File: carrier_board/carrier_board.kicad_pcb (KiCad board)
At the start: 2 copper layers, 40 x 68.9 mm, 10 parts, among them J1 47571-0001, U1 Pico

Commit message: Change red LED from GP2 to GP4 to free up UART RX
Also add label to LED on board
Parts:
- turned R1 to 90 degrees
- turned D1 to -90 degrees
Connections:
- D1 pad 1: Net-(D1-Pad1) -> GND
- D1 pad 2: Net-(D1-Pad2) -> Net-(R1-Pad2)
- R1 pad 1: Net-(D1-Pad1) -> Net-(U1-Pad6)
- R1 pad 2: GND -> Net-(R1-Pad2)
- U1 pad 2: Net-(D1-Pad2) -> unconnected-(U1-Pad2)
- U1 pad 6: unconnected-(U1-Pad6) -> Net-(U1-Pad6)
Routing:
- net Net-(D1-Pad2): track 9.67 -> 0.00 mm
- net Net-(U1-Pad6): track 0.00 -> 8.39 mm
- net Net-(R1-Pad2): track 0.00 -> 3.25 mm
- net Net-(D1-Pad1): track 3.21 -> 0.00 mm
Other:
- board text added: "OpenReset Carrier Board v1a caralynx 2022"
- board text removed: "OpenReset Carrier Board v1 caralynx 2022"

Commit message: Fix weird 3v3 routing
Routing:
- net VDD: track 55.9 -> 54.5 mm, vias 2 -> 1
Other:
- board text added: "OpenReset Carrier Board v1b caralynx 2022"
- board text removed: "OpenReset Carrier Board v1a caralynx 2022"
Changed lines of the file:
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@@
     (title "OpenReset Carrier Board")
     (date "2022-03-20")
-    (rev "v1a")
+    (rev "v1b")
     (company "cyanic")
   )
@@
   )
   (gr_rect (start 127 59) (end 167 127.9) (layer "Edge.Cuts") (width 0.1) (fill none))
-  (gr_text "OpenReset Carrier Board v1a\ncaralynx 2022" (at 147 120) (layer "B.SilkS")
+  (gr_text "OpenReset Carrier Board v1b\ncaralynx 2022" (at 147 120) (layer "B.SilkS")
     (effects (font (size 1 1) (thickness 0.15)) (justify mirror))
   )
@@
   (segment (start 151.8 117) (end 163 117) (width 0.25) (layer "F.Cu") (net 5))
   (segment (start 164 116) (end 164 101) (width 0.25) (layer "F.Cu") (net 5))
-  (segment (start 153.695 71.305) (end 153 72) (width 0.25) (layer "F.Cu") (net 6))
   (segment (start 153 116) (end 151 116) (width 0.25) (layer "F.Cu") (net 6))
   (segment (start 147.39 119.61) (end 147.39 121.06) (width 0.25) (layer "F.Cu") (net 6))
-  (segment (start 156.08 71.305) (end 153.695 71.305) (width 0.25) (layer "F.Cu") (net 6))
   (segment (start 151 116) (end 147.39 119.61) (width 0.25) (layer "F.Cu") (net 6))
   (via (at 153 116) (size 0.8) (drill 0.4) (layers "F.Cu" "B.Cu") (net 6))
-  (via (at 153 72) (size 0.8) (drill 0.4) (layers "F.Cu" "B.Cu") (net 6))
-  (segment (start 153 116) (end 153 72) (width 0.25) (layer "B.Cu") (net 6))
+  (segment (start 153 74.385) (end 153 116) (width 0.25) (layer "B.Cu") (net 6))
+  (segment (start 156.08 71.305) (end 153 74.385) (width 0.25) (layer "B.Cu") (net 6))
   (segment (start 161.785 101.785) (end 156.08 101.785) (width 0.25) (layer "F.Cu") (net 7))
   (segment (start 151 115) (end 162 115) (width 0.25) (layer "F.Cu") (net 7))

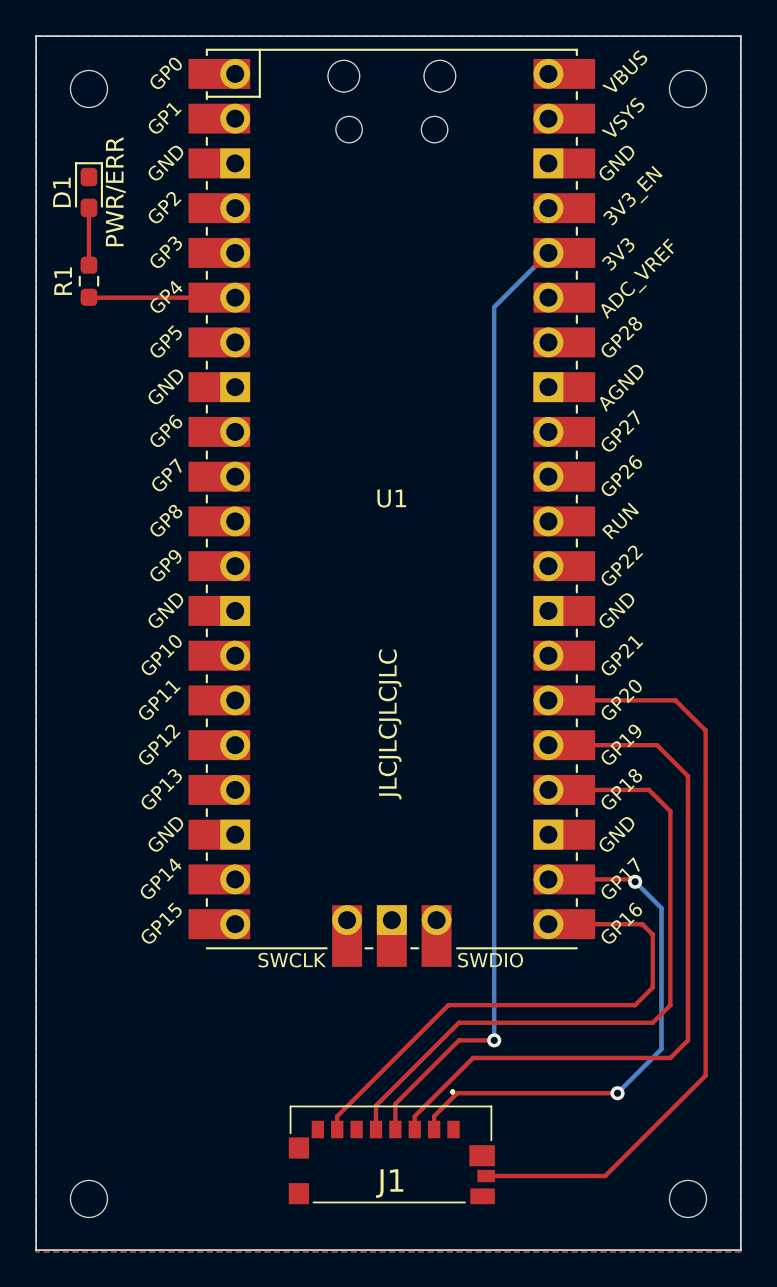
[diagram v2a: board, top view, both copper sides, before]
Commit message: Thicken power trace
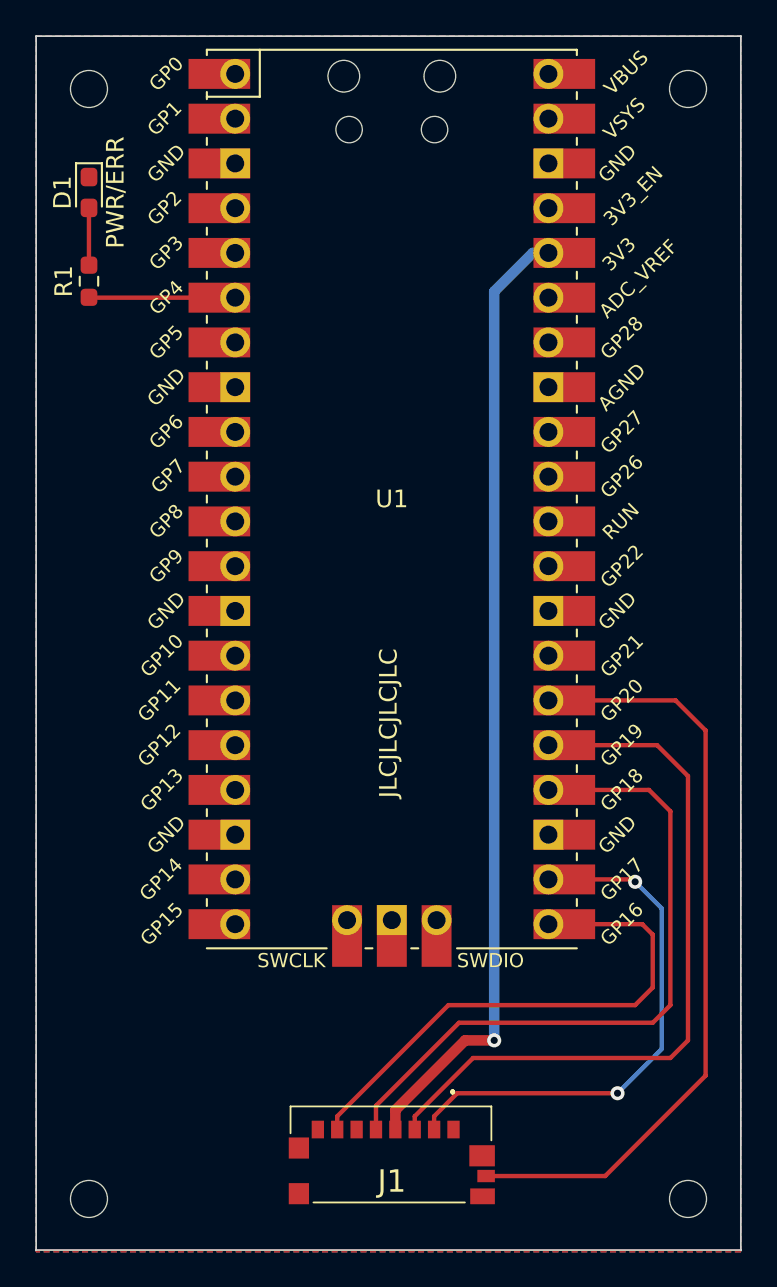
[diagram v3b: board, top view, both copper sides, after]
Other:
- board text added: "OpenReset Carrier Board v1c caralynx 2022"
- board text removed: "OpenReset Carrier Board v1b caralynx 2022"
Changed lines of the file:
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@@
   )
   (gr_rect (start 127 59) (end 167 127.9) (layer "Edge.Cuts") (width 0.1) (fill none))
-  (gr_text "OpenReset Carrier Board v1b\ncaralynx 2022" (at 147 120) (layer "B.SilkS")
+  (gr_text "OpenReset Carrier Board v1c\ncaralynx 2022" (at 147 120) (layer "B.SilkS")
     (effects (font (size 1 1) (thickness 0.15)) (justify mirror))
   )
@@
   (segment (start 151.8 117) (end 163 117) (width 0.25) (layer "F.Cu") (net 5))
   (segment (start 164 116) (end 164 101) (width 0.25) (layer "F.Cu") (net 5))
-  (segment (start 153 116) (end 151 116) (width 0.25) (layer "F.Cu") (net 6))
-  (segment (start 147.39 119.61) (end 147.39 121.06) (width 0.25) (layer "F.Cu") (net 6))
-  (segment (start 151 116) (end 147.39 119.61) (width 0.25) (layer "F.Cu") (net 6))
+  (segment (start 147.39 121.06) (end 147.39 119.96) (width 0.6) (layer "F.Cu") (net 6))
+  (segment (start 147.39 119.96) (end 151.35 116) (width 0.6) (layer "F.Cu") (net 6))
+  (segment (start 151.35 116) (end 153 116) (width 0.6) (layer "F.Cu") (net 6))
   (via (at 153 116) (size 0.8) (drill 0.4) (layers "F.Cu" "B.Cu") (net 6))
-  (segment (start 153 74.385) (end 153 116) (width 0.25) (layer "B.Cu") (net 6))
-  (segment (start 156.08 71.305) (end 153 74.385) (width 0.25) (layer "B.Cu") (net 6))
+  (segment (start 155.195 71.305) (end 156.08 71.305) (width 0.6) (layer "B.Cu") (net 6))
+  (segment (start 153 73.5) (end 155.195 71.305) (width 0.6) (layer "B.Cu") (net 6))
+  (segment (start 153 116) (end 153 73.5) (width 0.6) (layer "B.Cu") (net 6))
   (segment (start 161.785 101.785) (end 156.08 101.785) (width 0.25) (layer "F.Cu") (net 7))
   (segment (start 151 115) (end 162 115) (width 0.25) (layer "F.Cu") (net 7))
